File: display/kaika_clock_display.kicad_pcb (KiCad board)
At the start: 2 copper layers, 0 parts

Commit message: continue work on the display
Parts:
- added C1: 100nf, Capacitor_SMD:C_0805_2012Metric_Pad1.18x1.45mm_HandSolder, F.Cu at (120.5, 124.7)
- added C2: 100nf, Capacitor_SMD:C_0805_2012Metric_Pad1.18x1.45mm_HandSolder, F.Cu at (152.4, 124.7)
- added C3: 100nf, Capacitor_SMD:C_0805_2012Metric_Pad1.18x1.45mm_HandSolder, F.Cu at (184.8, 124.2)
- added C4: 100nf, Capacitor_SMD:C_0805_2012Metric_Pad1.18x1.45mm_HandSolder, F.Cu at (216.6, 124.6)
- added H1: MountingHole, MountingHole:MountingHole_2.2mm_M2_DIN965_Pad, F.Cu at (103.0, 106.0)
- added H2: MountingHole, MountingHole:MountingHole_2.2mm_M2_DIN965_Pad, F.Cu at (225.0, 106.0)
- added H3: MountingHole, MountingHole:MountingHole_2.2mm_M2_DIN965_Pad, F.Cu at (225.0, 126.0)
- added H4: MountingHole, MountingHole:MountingHole_2.2mm_M2_DIN965_Pad, F.Cu at (103.0, 126.0)
- added J1: Conn_01x05, Connector_PinHeader_1.27mm:PinHeader_1x06_P1.27mm_Vertical, B.Cu at (103.0, 111.1)
- added R1: 10K, Resistor_SMD:R_0805_2012Metric_Pad1.20x1.40mm_HandSolder, F.Cu at (116.0, 124.6)
- added R2: 10K, Resistor_SMD:R_0805_2012Metric_Pad1.20x1.40mm_HandSolder, F.Cu at (148.2, 124.7)
- added R3: 10K, Resistor_SMD:R_0805_2012Metric_Pad1.20x1.40mm_HandSolder, F.Cu at (180.4, 124.4)
- added R4: 10K, Resistor_SMD:R_0805_2012Metric_Pad1.20x1.40mm_HandSolder, F.Cu at (212.3, 124.6)
- added U1: MAX7219, Package_SO:SOIC-24W_7.5x15.4mm_P1.27mm, F.Cu at (116.0, 116.0)
- added U2: MAX7219, Package_SO:SOIC-24W_7.5x15.4mm_P1.27mm, F.Cu at (148.0, 116.0)
- added U3: MAX7219, Package_SO:SOIC-24W_7.5x15.4mm_P1.27mm, F.Cu at (180.0, 116.0)
- added U4: MAX7219, Package_SO:SOIC-24W_7.5x15.4mm_P1.27mm, F.Cu at (212.0, 116.0)
- added U5: LED-MATRIX-1088AS, Kaka-footprints:LED-DISPLAY-1088AS, F.Cu at (116.0, 116.0)
- added U6: LED-MATRIX-1088AS, Kaka-footprints:LED-DISPLAY-1088AS, F.Cu at (148.0, 116.0)
- added U7: LED-MATRIX-1088AS, Kaka-footprints:LED-DISPLAY-1088AS, F.Cu at (180.0, 116.0)
- added U8: LED-MATRIX-1088AS, Kaka-footprints:LED-DISPLAY-1088AS, F.Cu at (212.0, 116.0)
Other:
- board outline added: 128 x 32 mm

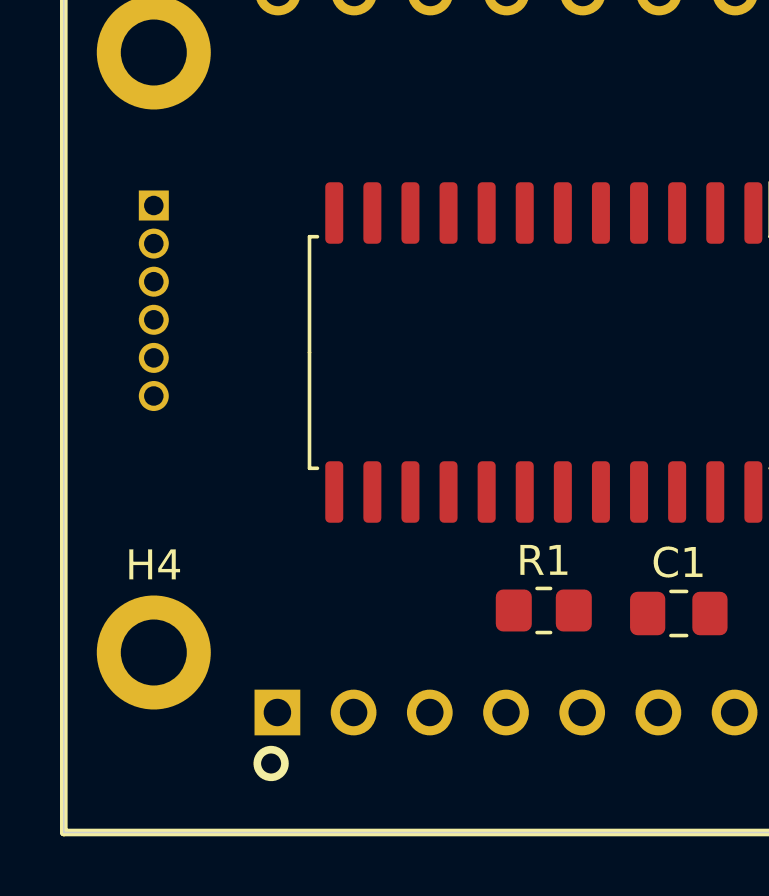
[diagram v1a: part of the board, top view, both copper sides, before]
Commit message: modify the main and display
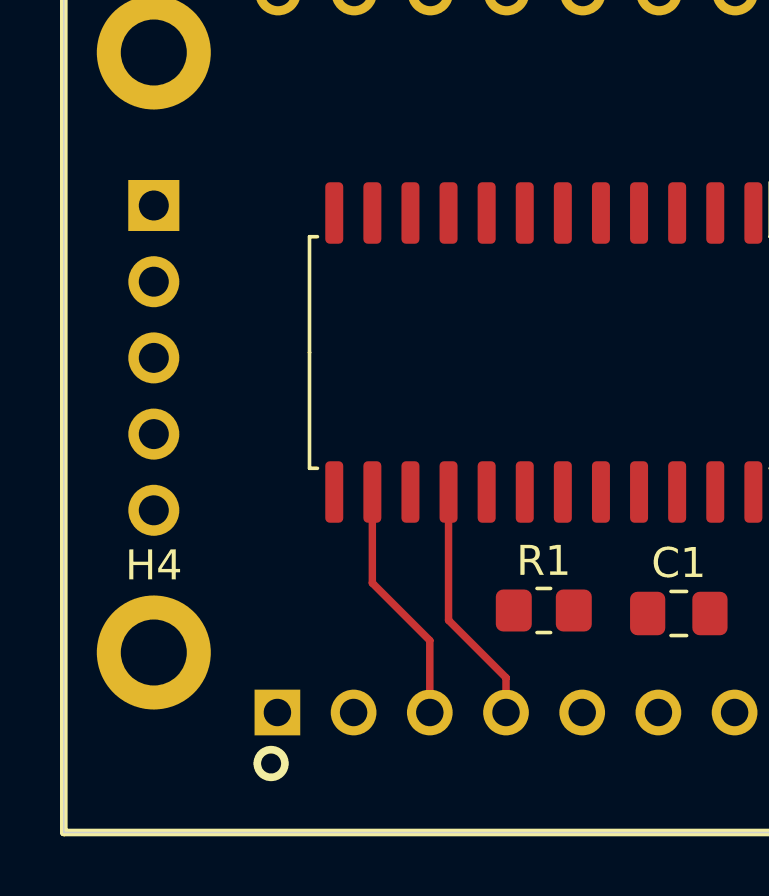
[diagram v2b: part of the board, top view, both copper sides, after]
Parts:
- J1: footprint Connector_PinHeader_1.27mm:PinHeader_1x06_P1.27mm_Vertical -> Connector_PinHeader_2.54mm:PinHeader_1x05_P2.54mm_Vertical
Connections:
- J1 pad 1: CLK -> GND
- J1 pad 2: DIN -> +3V3
- J1 pad 4: GND -> DIN
- J1 pad 5: +3V3 -> CLK
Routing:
- net 1_SEG_B: track 0.00 -> 8.14 mm
- net 1_SEG_A: track 0.00 -> 8.14 mm

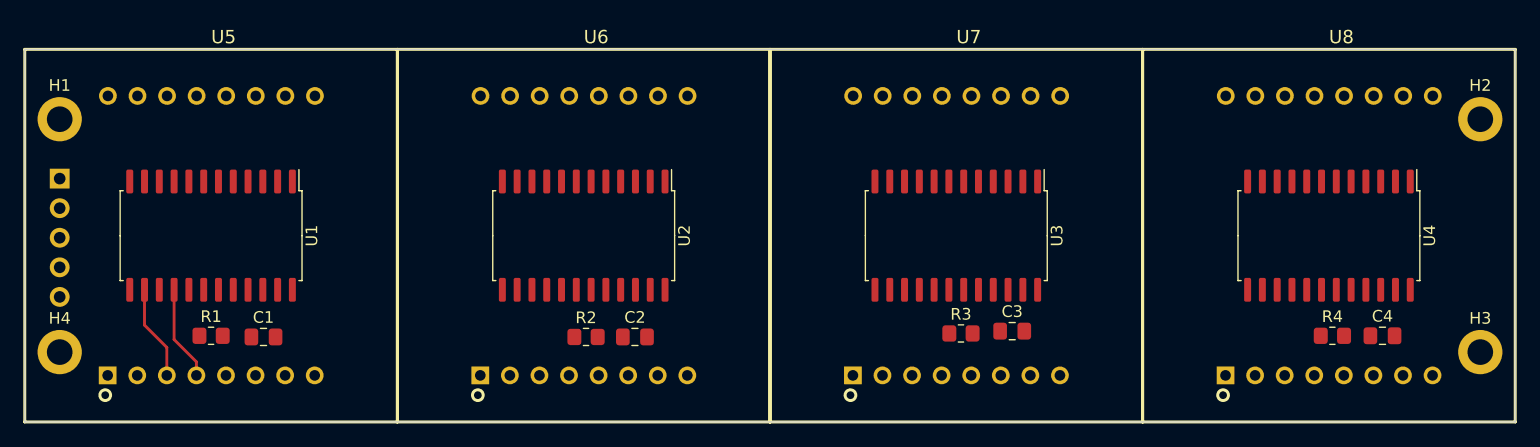
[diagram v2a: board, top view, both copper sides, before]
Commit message: change usb footprint
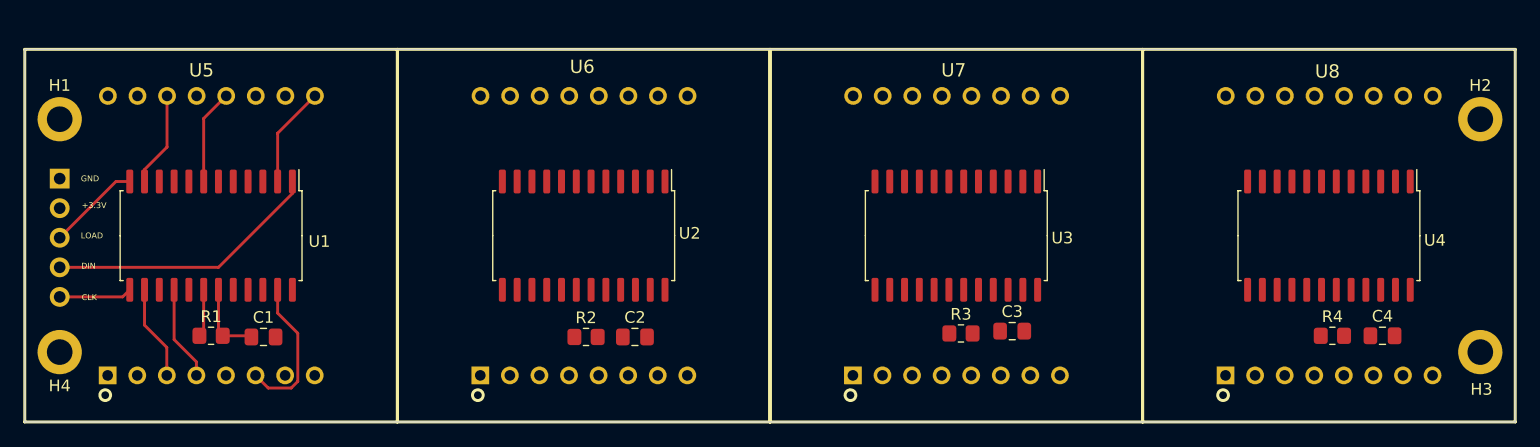
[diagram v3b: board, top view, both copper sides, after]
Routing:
- net DIN: track 0.00 -> 23.6 mm
- net 1_SEG_D: track 0.00 -> 12.9 mm
- net 1_DIG_0: track 0.00 -> 8.68 mm
- net 1_DIG_3: track 0.00 -> 8.15 mm
- net 1_DIG_1: track 0.00 -> 8.15 mm
- net LOAD: track 0.00 -> 8.02 mm
- net +3V3: track 0.00 -> 6.61 mm
- net CLK: track 0.00 -> 6.27 mm
- net Net-(R1-Pad1): track 0.00 -> 4.10 mm
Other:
- board text added: "+3.3V"
- board text added: "CLK"
- board text added: "DIN"
- board text added: "GND"
- board text added: "LOAD"

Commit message: finish display board draw.
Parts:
- moved C4 18.8 mm to (197.8, 124.4), turned to 180 degrees
- moved C3 18.8 mm to (166.1, 124.6), turned to 180 degrees
- moved C2 18.5 mm to (133.9, 124.5), turned to 180 degrees
- moved C1 13.4 mm to (107.1, 124.0), turned to 180 degrees
- moved R4 10.7 mm to (201.6, 124.4), turned to 180 degrees
- moved R3 10.5 mm to (169.9, 124.6), turned to 180 degrees
- moved R2 10.1 mm to (138.1, 124.5), turned to 180 degrees
- moved R1 5.04 mm to (111.0, 124.0), turned to 180 degrees
- turned U5 to 180 degrees
- turned U6 to 180 degrees
- turned U7 to 180 degrees
- turned U8 to 180 degrees
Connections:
- H1 pad 1: (no net) -> GND
- H4 pad 1: (no net) -> GND
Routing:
- net GND: track 0.00 -> 307.9 mm
- net +3V3: track 6.61 -> 183.4 mm
- net LOAD: track 8.02 -> 134.4 mm
- net CLK: track 6.27 -> 124.5 mm, vias 0 -> 1
- net Net-(U3-Pad24): track 0.00 -> 59.3 mm
- net 4_DIG_0: track 0.00 -> 38.8 mm
- net 1_DIG_0: track 8.68 -> 47.4 mm
- net Net-(U1-Pad24): track 0.00 -> 36.5 mm
- net Net-(U2-Pad24): track 0.00 -> 36.1 mm
- net 4_SEG_A: track 0.00 -> 33.8 mm
- net 1_SEG_F: track 0.00 -> 29.9 mm
- net 3_SEG_F: track 0.00 -> 28.1 mm
- net 2_SEG_A: track 0.00 -> 27.4 mm, vias 0 -> 1
- net 3_DIG_0: track 0.00 -> 27.0 mm, vias 0 -> 1
- net 3_SEG_D: track 0.00 -> 26.9 mm, vias 0 -> 1
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- added copper zone on B.Cu, net GND
- added copper zone on F.Cu, net GND

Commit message: finish the project
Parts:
- moved R2 4.04 mm to (134.5, 126.4), turned to 90 degrees
- moved R3 3.49 mm to (166.6, 125.8), turned to 90 degrees
- moved R4 3.05 mm to (198.9, 125.7), turned to 90 degrees
- moved C3 2.73 mm to (166.6, 122.0), turned to 90 degrees
- moved C4 2.67 mm to (198.9, 121.9), turned to 90 degrees
- moved C2 2.42 mm to (134.5, 122.2), turned to 90 degrees
- moved R1 2.34 mm to (108.8, 124.8), turned to 270 degrees
- moved C1 0.89 mm to (106.7, 124.8), turned to 90 degrees
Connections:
- H4 pad 1: GND -> (no net)
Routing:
- net GND: track 307.9 -> 234.7 mm, vias 0 -> 13
- net +3V3: track 183.4 -> 215.6 mm, vias 0 -> 20
- net DIN: track 23.3 -> 53.1 mm
- net Net-(U3-Pad24): track 59.3 -> 38.5 mm
- net 1_DIG_3: track 24.1 -> 41.5 mm
- net LOAD: track 134.4 -> 119.7 mm, vias 0 -> 4
- net 1_SEG_F: track 29.9 -> 15.4 mm, vias 0 -> 1
- net Net-(U1-Pad24): track 36.5 -> 50.6 mm
- net 1_SEG_A: track 34.5 -> 21.2 mm, vias 0 -> 1
- net 3_SEG_F: track 28.1 -> 15.3 mm, vias 0 -> 1
- net 4_SEG_A: track 33.8 -> 22.4 mm, vias 0 -> 1
- net 4_SEG_G: track 26.6 -> 16.0 mm, vias 0 -> 1
- net Net-(R1-Pad1): track 5.02 -> 15.5 mm, vias 0 -> 2
- net 2_SEG_G: track 26.6 -> 16.2 mm, vias 0 -> 1
- net 2_SEG_B: track 18.5 -> 28.5 mm, vias 1 -> 0
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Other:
- board text added: "20201229"
- board text added: "Kaika Team"
- board text added: "V1.0"

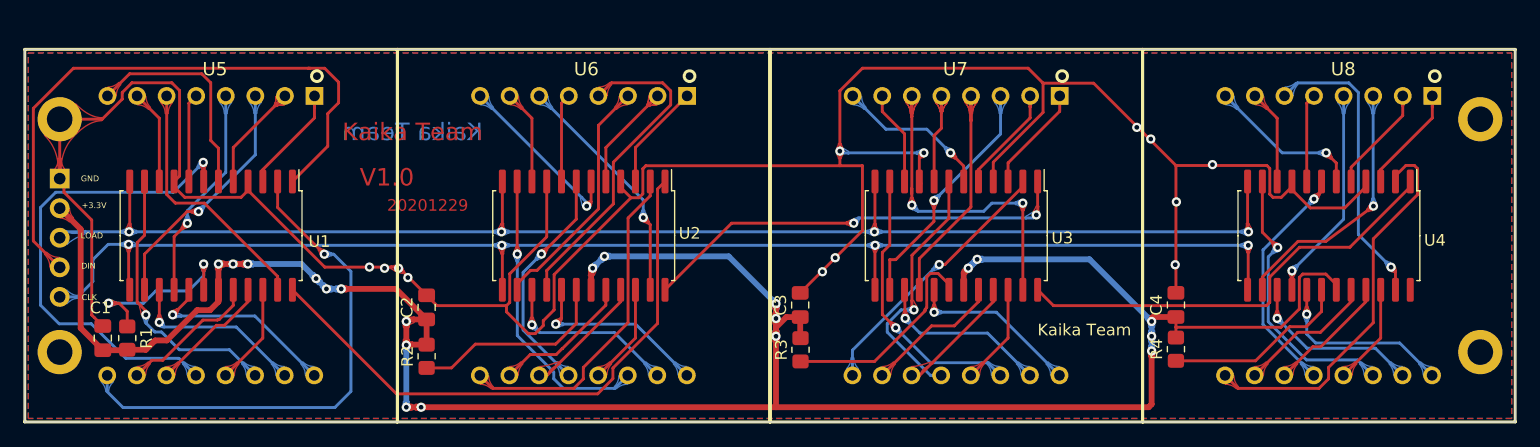
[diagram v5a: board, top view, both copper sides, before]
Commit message: modify the main and display
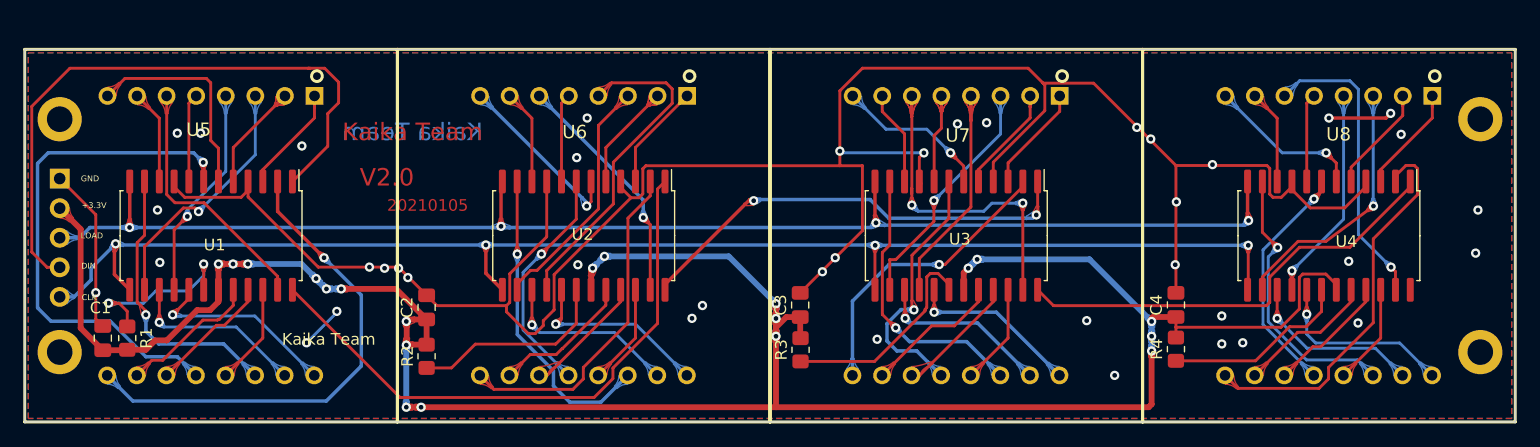
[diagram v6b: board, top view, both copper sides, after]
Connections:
- net +3V3 renamed VCC
- H2 pad 1: (no net) -> GND
- H3 pad 1: (no net) -> GND
- H4 pad 1: (no net) -> GND
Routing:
- net GND: track 234.7 -> 219.1 mm, vias 13 -> 41
- net 1_DIG_3: track 41.5 -> 45.0 mm
- net 3_DIG_0: track 23.1 -> 25.6 mm
- net 1_DIG_0: track 44.6 -> 42.8 mm
- net Net-(U2-Pad24): track 37.5 -> 39.2 mm
- net CLK: track 120.8 -> 122.2 mm
- net 2_DIG_1: track 25.4 -> 26.8 mm
- net LOAD: track 119.7 -> 118.5 mm
- net DIN: track 53.1 -> 54.0 mm
- net 1_SEG_A: track 21.2 -> 21.8 mm
- net 3_DIG_3: track 22.1 -> 22.6 mm
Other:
- board text added: "20210105"
- board text added: "Kaika Team V2.0"
- board text added: "V2.0"
- board text added: "VCC"
- board text removed: "20201229"
- board text removed: "V1.0"

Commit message: modify the display
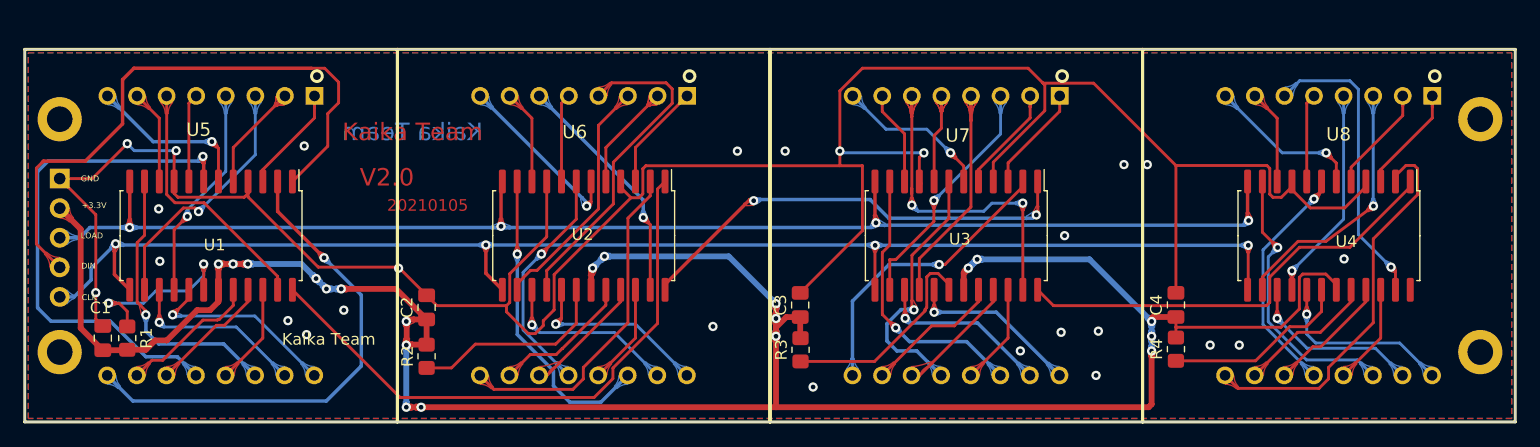
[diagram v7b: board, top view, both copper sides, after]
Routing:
- net GND: track 219.1 -> 225.0 mm, vias 41 -> 26
- net 1_DIG_2: track 18.4 -> 14.4 mm, vias 0 -> 1
- net DIN: track 54.0 -> 51.9 mm

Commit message: modify diplay
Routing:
- net GND: track 225.0 -> 237.9 mm, vias 26 -> 47
- net 4_DIG_0: track 33.8 -> 42.5 mm
- net 2_DIG_1: track 26.8 -> 28.7 mm
- net 3_DIG_3: track 22.6 -> 24.4 mm
- net Net-(R3-Pad1): track 18.4 -> 16.9 mm
- net 4_SEG_D: track 25.7 -> 26.8 mm
- net 2_DIG_4: track 10.0 -> 10.9 mm
